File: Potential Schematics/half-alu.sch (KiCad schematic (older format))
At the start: 4 parts

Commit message: Made Full ALU
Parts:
- gave numbers to parts that had none: 4
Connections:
- net 1:2_Multiplexer/Out: now also U2.5; no longer U2.2
- net 2:4_Multiplexer/D0: now also U2.6; no longer U2.3
- net b: now also U2.4; no longer U2.1
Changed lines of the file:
@@
 $Descr A4 11693 8268
 encoding utf-8
-Sheet 3 6
+Sheet 7 22
 Title "Half-ALU"
 Date ""
@@
 $Comp
 L 74LS08 U?
-U 1 1 5B989249
+U 2 1 5B989249
 P 6250 2300
 AR Path="/5B987476/5B989249" Ref="U?"  Part="1"
-AR Path="/5B990C59/5B990C5E/5B989249" Ref="U?"  Part="1"
-F 0 "U?" H 6250 2350 50  0000 C CNN
+AR Path="/5B990C59/5B990C5E/5B989249" Ref="U2"  Part="1"
+AR Path="/5B990C59/5B99C8B8/5B989249" Ref="U21"  Part="4"
+AR Path="/5B990C59/5B99BC00/5B989249" Ref="U5"  Part="2"
+AR Path="/5B990C59/5B99C896/5B989249" Ref="U13"  Part="3"
+F 0 "U5" H 6250 2350 50  0000 C CNN
 F 1 "74LS08" H 6250 2250 50  0000 C CNN
 F 2 "" H 6250 2300 50  0001 C CNN
 F 3 "" H 6250 2300 50  0001 C CNN
-	1    6250 2300
+	2    6250 2300
 	1    0    0    -1
 $EndComp
@@
 P 6250 2800
 AR Path="/5B987476/5B98940C" Ref="U?"  Part="1"
-AR Path="/5B990C59/5B990C5E/5B98940C" Ref="U?"  Part="1"
-F 0 "U?" H 6250 2850 50  0000 C CNN
+AR Path="/5B990C59/5B990C5E/5B98940C" Ref="U3"  Part="1"
+AR Path="/5B990C59/5B99C8B8/5B98940C" Ref="U26"  Part="1"
+AR Path="/5B990C59/5B99BC00/5B98940C" Ref="U11"  Part="1"
+AR Path="/5B990C59/5B99C896/5B98940C" Ref="U19"  Part="1"
+F 0 "U11" H 6250 2850 50  0000 C CNN
 F 1 "74LS32" H 6250 2750 50  0000 C CNN
 F 2 "" H 6250 2800 50  0001 C CNN
@@
 P 6250 3350
 AR Path="/5B987476/5B98B405" Ref="U?"  Part="1"
-AR Path="/5B990C59/5B990C5E/5B98B405" Ref="U?"  Part="1"
-F 0 "U?" H 6300 3400 50  0000 C CNN
+AR Path="/5B990C59/5B990C5E/5B98B405" Ref="U4"  Part="1"
+AR Path="/5B990C59/5B99C8B8/5B98B405" Ref="U27"  Part="1"
+AR Path="/5B990C59/5B99BC00/5B98B405" Ref="U12"  Part="1"
+AR Path="/5B990C59/5B99C896/5B98B405" Ref="U20"  Part="1"
+F 0 "U12" H 6300 3400 50  0000 C CNN
 F 1 "74LS86" H 6300 3300 50  0000 C CNN
 F 2 "" H 6250 3350 50  0001 C CNN
@@
 P 2350 4000
 AR Path="/5B987476/5B98D385" Ref="U?"  Part="1"
-AR Path="/5B990C59/5B990C5E/5B98D385" Ref="U?"  Part="1"
-F 0 "U?" H 2545 4115 50  0000 C CNN
+AR Path="/5B990C59/5B990C5E/5B98D385" Ref="U1"  Part="1"
+AR Path="/5B990C59/5B99C8B8/5B98D385" Ref="U25"  Part="1"
+AR Path="/5B990C59/5B99BC00/5B98D385" Ref="U10"  Part="1"
+AR Path="/5B990C59/5B99C896/5B98D385" Ref="U18"  Part="1"
+F 0 "U10" H 2545 4115 50  0000 C CNN
 F 1 "74LS04" H 2540 3875 50  0000 C CNN
 F 2 "" H 2350 4000 50  0001 C CNN
@@
 $EndSheet
 $Sheet
-S 8100 3300 550  850
+S 8100 3450 550  700
 U 5B98E051
 F0 "2:4_Multiplexer" 60
@@
 Connection ~ 4600 2900
 Wire Wire Line
-	1650 2700 2050 2700
+	1650 2700 5650 2700
 Wire Wire Line
 	2050 2200 2050 3250
 Wire Wire Line
 	2050 2200 5650 2200
-Wire Wire Line
-	2050 2700 5650 2700
 Connection ~ 2050 2700
 Wire Wire Line
@@
 Wire Wire Line
 	5150 4000 5650 4000
+Connection ~ 1900 4000
 $EndSCHEMATC

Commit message: Adding Multiply Devide
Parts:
- U1: symbol 74LS04 -> 4-bit_processor-rescue:74LS04
- U2: symbol 74LS08 -> 4-bit_processor-rescue:74LS08
- U3: symbol 74LS32 -> 4-bit_processor-rescue:74LS32
- U4: symbol 74LS86 -> 4-bit_processor-rescue:74LS86
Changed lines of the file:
@@
-EESchema Schematic File Version 2
-LIBS:power
-LIBS:device
-LIBS:switches
-LIBS:relays
-LIBS:motors
-LIBS:transistors
-LIBS:conn
-LIBS:linear
-LIBS:regul
-LIBS:74xx
-LIBS:cmos4000
-LIBS:adc-dac
-LIBS:memory
-LIBS:xilinx
-LIBS:microcontrollers
-LIBS:dsp
-LIBS:microchip
-LIBS:analog_switches
-LIBS:motorola
-LIBS:texas
-LIBS:intel
-LIBS:audio
-LIBS:interface
-LIBS:digital-audio
-LIBS:philips
-LIBS:display
-LIBS:cypress
-LIBS:siliconi
-LIBS:opto
-LIBS:atmel
-LIBS:contrib
-LIBS:valves
+EESchema Schematic File Version 4
 LIBS:4-bit_processor-cache
-EELAYER 25 0
+EELAYER 26 0
 EELAYER END
 $Descr A4 11693 8268
 encoding utf-8
-Sheet 7 449
+Sheet 4 451
 Title "Half-ALU"
 Date "2018-09-14"
@@
 $EndSheet
 $Comp
-L 74LS08 U?
+L 4-bit_processor-rescue:74LS08 U?
 U 2 1 5B989249
 P 6250 2300
@@
 $EndComp
 $Comp
-L 74LS32 U?
+L 4-bit_processor-rescue:74LS32 U?
 U 1 1 5B98940C
 P 6250 2800
@@
 $EndComp
 $Comp
-L 74LS86 U?
+L 4-bit_processor-rescue:74LS86 U?
 U 1 1 5B98B405
 P 6250 3350
@@
 a
 $Comp
-L 74LS04 U?
+L 4-bit_processor-rescue:74LS04 U?
 U 1 1 5B98D385
 P 2350 4000
@@
 	4600 4200 3950 4200
 Wire Wire Line
-	4600 2400 4600 4400
+	4600 2400 4600 2900
 Wire Wire Line
 	4600 3450 5650 3450
@@
 Connection ~ 4600 2900
 Wire Wire Line
-	1650 2700 5650 2700
-Wire Wire Line
-	2050 2200 2050 3250
+	1650 2700 2050 2700
+Wire Wire Line
+	2050 2200 2050 2700
 Wire Wire Line
 	2050 2200 5650 2200
 Connection ~ 2050 2700
 Wire Wire Line
-	2050 3250 5650 3250
+	2050 3250 5050 3250
 Text HLabel 6700 5500 3    60   Output ~ 0
 Cout
@@
 	5150 4000 5650 4000
 Connection ~ 1900 4000
+Wire Wire Line
+	4600 3450 4600 4200
+Wire Wire Line
+	4600 2900 4600 3450
+Wire Wire Line
+	2050 2700 5650 2700
+Wire Wire Line
+	2050 2700 2050 3250
+Wire Wire Line
+	5050 3250 5650 3250
+Wire Wire Line
+	4600 4200 4600 4400
 $EndSCHEMATC

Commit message: Finished PCB
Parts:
- U1: renamed from U2; footprint (none) -> Daniel_Kopp:DIP-14_300_ELL
- U2: renamed from U1; footprint (none) -> Daniel_Kopp:DIP-14_300_ELL
- U3, U4: footprint (none) -> Daniel_Kopp:DIP-14_300_ELL
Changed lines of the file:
@@
 $Descr A4 11693 8268
 encoding utf-8
-Sheet 4 451
+Sheet 4 456
 Title "Half-ALU"
 Date "2018-09-14"
@@
 P 6250 2300
 AR Path="/5B987476/5B989249" Ref="U?"  Part="1"
-AR Path="/5B990C59/5B990C5E/5B989249" Ref="U2"  Part="1"
-AR Path="/5B990C59/5B99C8B8/5B989249" Ref="U21"  Part="4"
-AR Path="/5B990C59/5B99BC00/5B989249" Ref="U5"  Part="2"
-AR Path="/5B990C59/5B99C896/5B989249" Ref="U13"  Part="3"
-AR Path="/5B9D167A/5B9D1E00/5B990C5E/5B989249" Ref="U5"  Part="2"
-AR Path="/5B9D167A/5B9D1E00/5B99BC00/5B989249" Ref="U5"  Part="2"
-AR Path="/5B9D167A/5B9D1E00/5B99C896/5B989249" Ref="U5"  Part="2"
-AR Path="/5B9D167A/5B9D1E00/5B99C8B8/5B989249" Ref="U5"  Part="2"
-F 0 "U5" H 6250 2350 50  0000 C CNN
+AR Path="/5B990C59/5B990C5E/5B989249" Ref="U?"  Part="1"
+AR Path="/5B990C59/5B99C8B8/5B989249" Ref="U?"  Part="4"
+AR Path="/5B990C59/5B99BC00/5B989249" Ref="U?"  Part="2"
+AR Path="/5B990C59/5B99C896/5B989249" Ref="U?"  Part="3"
+AR Path="/5B9D167A/5B9D1E00/5B990C5E/5B989249" Ref="U1"  Part="2"
+AR Path="/5B9D167A/5B9D1E00/5B99BC00/5B989249" Ref="U5"  Part="3"
+AR Path="/5B9D167A/5B9D1E00/5B99C896/5B989249" Ref="U10"  Part="4"
+AR Path="/5B9D167A/5B9D1E00/5B99C8B8/5B989249" Ref="U19"  Part="1"
+F 0 "U1" H 6250 2350 50  0000 C CNN
 F 1 "74LS08" H 6250 2250 50  0000 C CNN
-F 2 "" H 6250 2300 50  0001 C CNN
+F 2 "Daniel_Kopp:DIP-14_300_ELL" H 6250 2300 50  0001 C CNN
 F 3 "" H 6250 2300 50  0001 C CNN
 	2    6250 2300
@@
 P 6250 2800
 AR Path="/5B987476/5B98940C" Ref="U?"  Part="1"
-AR Path="/5B990C59/5B990C5E/5B98940C" Ref="U3"  Part="1"
-AR Path="/5B990C59/5B99C8B8/5B98940C" Ref="U26"  Part="1"
-AR Path="/5B990C59/5B99BC00/5B98940C" Ref="U11"  Part="1"
-AR Path="/5B990C59/5B99C896/5B98940C" Ref="U19"  Part="1"
-AR Path="/5B9D167A/5B9D1E00/5B990C5E/5B98940C" Ref="U11"  Part="1"
-AR Path="/5B9D167A/5B9D1E00/5B99BC00/5B98940C" Ref="U11"  Part="1"
-AR Path="/5B9D167A/5B9D1E00/5B99C896/5B98940C" Ref="U11"  Part="1"
-AR Path="/5B9D167A/5B9D1E00/5B99C8B8/5B98940C" Ref="U11"  Part="1"
-F 0 "U11" H 6250 2850 50  0000 C CNN
+AR Path="/5B990C59/5B990C5E/5B98940C" Ref="U?"  Part="1"
+AR Path="/5B990C59/5B99C8B8/5B98940C" Ref="U?"  Part="1"
+AR Path="/5B990C59/5B99BC00/5B98940C" Ref="U?"  Part="1"
+AR Path="/5B990C59/5B99C896/5B98940C" Ref="U?"  Part="1"
+AR Path="/5B9D167A/5B9D1E00/5B990C5E/5B98940C" Ref="U3"  Part="1"
+AR Path="/5B9D167A/5B9D1E00/5B99BC00/5B98940C" Ref="U8"  Part="2"
+AR Path="/5B9D167A/5B9D1E00/5B99C896/5B98940C" Ref="U13"  Part="3"
+AR Path="/5B9D167A/5B9D1E00/5B99C8B8/5B98940C" Ref="U17"  Part="4"
+F 0 "U3" H 6250 2850 50  0000 C CNN
 F 1 "74LS32" H 6250 2750 50  0000 C CNN
-F 2 "" H 6250 2800 50  0001 C CNN
+F 2 "Daniel_Kopp:DIP-14_300_ELL" H 6250 2800 50  0001 C CNN
 F 3 "" H 6250 2800 50  0001 C CNN
 	1    6250 2800
@@
 P 6250 3350
 AR Path="/5B987476/5B98B405" Ref="U?"  Part="1"
-AR Path="/5B990C59/5B990C5E/5B98B405" Ref="U4"  Part="1"
-AR Path="/5B990C59/5B99C8B8/5B98B405" Ref="U27"  Part="1"
-AR Path="/5B990C59/5B99BC00/5B98B405" Ref="U12"  Part="1"
-AR Path="/5B990C59/5B99C896/5B98B405" Ref="U20"  Part="1"
-AR Path="/5B9D167A/5B9D1E00/5B990C5E/5B98B405" Ref="U12"  Part="1"
-AR Path="/5B9D167A/5B9D1E00/5B99BC00/5B98B405" Ref="U12"  Part="1"
-AR Path="/5B9D167A/5B9D1E00/5B99C896/5B98B405" Ref="U12"  Part="1"
-AR Path="/5B9D167A/5B9D1E00/5B99C8B8/5B98B405" Ref="U12"  Part="1"
-F 0 "U12" H 6300 3400 50  0000 C CNN
+AR Path="/5B990C59/5B990C5E/5B98B405" Ref="U?"  Part="1"
+AR Path="/5B990C59/5B99C8B8/5B98B405" Ref="U?"  Part="1"
+AR Path="/5B990C59/5B99BC00/5B98B405" Ref="U?"  Part="1"
+AR Path="/5B990C59/5B99C896/5B98B405" Ref="U?"  Part="1"
+AR Path="/5B9D167A/5B9D1E00/5B990C5E/5B98B405" Ref="U4"  Part="1"
+AR Path="/5B9D167A/5B9D1E00/5B99BC00/5B98B405" Ref="U9"  Part="1"
+AR Path="/5B9D167A/5B9D1E00/5B99C896/5B98B405" Ref="U14"  Part="1"
+AR Path="/5B9D167A/5B9D1E00/5B99C8B8/5B98B405" Ref="U20"  Part="1"
+F 0 "U4" H 6300 3400 50  0000 C CNN
 F 1 "74LS86" H 6300 3300 50  0000 C CNN
-F 2 "" H 6250 3350 50  0001 C CNN
+F 2 "Daniel_Kopp:DIP-14_300_ELL" H 6250 3350 50  0001 C CNN
 F 3 "" H 6250 3350 50  0001 C CNN
 	1    6250 3350
@@
 P 2350 4000
 AR Path="/5B987476/5B98D385" Ref="U?"  Part="1"
-AR Path="/5B990C59/5B990C5E/5B98D385" Ref="U1"  Part="1"
-AR Path="/5B990C59/5B99C8B8/5B98D385" Ref="U25"  Part="1"
-AR Path="/5B990C59/5B99BC00/5B98D385" Ref="U10"  Part="1"
-AR Path="/5B990C59/5B99C896/5B98D385" Ref="U18"  Part="1"
-AR Path="/5B9D167A/5B9D1E00/5B990C5E/5B98D385" Ref="U10"  Part="1"
-AR Path="/5B9D167A/5B9D1E00/5B99BC00/5B98D385" Ref="U10"  Part="1"
-AR Path="/5B9D167A/5B9D1E00/5B99C896/5B98D385" Ref="U10"  Part="1"
-AR Path="/5B9D167A/5B9D1E00/5B99C8B8/5B98D385" Ref="U10"  Part="1"
-F 0 "U10" H 2545 4115 50  0000 C CNN
+AR Path="/5B990C59/5B990C5E/5B98D385" Ref="U?"  Part="1"
+AR Path="/5B990C59/5B99C8B8/5B98D385" Ref="U?"  Part="1"
+AR Path="/5B990C59/5B99BC00/5B98D385" Ref="U?"  Part="1"
+AR Path="/5B990C59/5B99C896/5B98D385" Ref="U?"  Part="1"
+AR Path="/5B9D167A/5B9D1E00/5B990C5E/5B98D385" Ref="U2"  Part="1"
+AR Path="/5B9D167A/5B9D1E00/5B99BC00/5B98D385" Ref="U2"  Part="5"
+AR Path="/5B9D167A/5B9D1E00/5B99C896/5B98D385" Ref="U11"  Part="3"
+AR Path="/5B9D167A/5B9D1E00/5B99C8B8/5B98D385" Ref="U18"  Part="1"
+F 0 "U2" H 2545 4115 50  0000 C CNN
 F 1 "74LS04" H 2540 3875 50  0000 C CNN
-F 2 "" H 2350 4000 50  0001 C CNN
+F 2 "Daniel_Kopp:DIP-14_300_ELL" H 2350 4000 50  0001 C CNN
 F 3 "" H 2350 4000 50  0001 C CNN
 	1    2350 4000

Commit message: Working on Multiplier
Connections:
- net 1:2_Multiplexer/Out: now also U1.2, U3.13; no longer U1.5, U3.2
- net 2:4_Multiplexer/D0: now also U1.3; no longer U1.6
- net 2:4_Multiplexer/D1: now also U3.11; no longer U3.3
- net b: now also U1.1, U3.12; no longer U1.4, U3.1
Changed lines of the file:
@@
 $Descr A4 11693 8268
 encoding utf-8
-Sheet 4 456
+Sheet 16 458
 Title "Half-ALU"
 Date "2018-09-14"
@@
 $Comp
 L 4-bit_processor-rescue:74LS08 U?
-U 2 1 5B989249
+U 1 1 5B989249
 P 6250 2300
 AR Path="/5B987476/5B989249" Ref="U?"  Part="1"
@@
 AR Path="/5B9D167A/5B9D1E00/5B99C896/5B989249" Ref="U10"  Part="4"
 AR Path="/5B9D167A/5B9D1E00/5B99C8B8/5B989249" Ref="U19"  Part="1"
-F 0 "U1" H 6250 2350 50  0000 C CNN
+F 0 "U19" H 6250 2350 50  0000 C CNN
 F 1 "74LS08" H 6250 2250 50  0000 C CNN
 F 2 "Daniel_Kopp:DIP-14_300_ELL" H 6250 2300 50  0001 C CNN
 F 3 "" H 6250 2300 50  0001 C CNN
-	2    6250 2300
+	1    6250 2300
 	1    0    0    -1
 $EndComp
 $Comp
 L 4-bit_processor-rescue:74LS32 U?
-U 1 1 5B98940C
+U 4 1 5B98940C
 P 6250 2800
 AR Path="/5B987476/5B98940C" Ref="U?"  Part="1"
@@
 AR Path="/5B9D167A/5B9D1E00/5B99C896/5B98940C" Ref="U13"  Part="3"
 AR Path="/5B9D167A/5B9D1E00/5B99C8B8/5B98940C" Ref="U17"  Part="4"
-F 0 "U3" H 6250 2850 50  0000 C CNN
+F 0 "U17" H 6250 2850 50  0000 C CNN
 F 1 "74LS32" H 6250 2750 50  0000 C CNN
 F 2 "Daniel_Kopp:DIP-14_300_ELL" H 6250 2800 50  0001 C CNN
 F 3 "" H 6250 2800 50  0001 C CNN
-	1    6250 2800
+	4    6250 2800
 	1    0    0    -1
 $EndComp
@@
 AR Path="/5B9D167A/5B9D1E00/5B99C896/5B98B405" Ref="U14"  Part="1"
 AR Path="/5B9D167A/5B9D1E00/5B99C8B8/5B98B405" Ref="U20"  Part="1"
-F 0 "U4" H 6300 3400 50  0000 C CNN
+F 0 "U20" H 6300 3400 50  0000 C CNN
 F 1 "74LS86" H 6300 3300 50  0000 C CNN
 F 2 "Daniel_Kopp:DIP-14_300_ELL" H 6250 3350 50  0001 C CNN
@@
 AR Path="/5B9D167A/5B9D1E00/5B99C896/5B98D385" Ref="U11"  Part="3"
 AR Path="/5B9D167A/5B9D1E00/5B99C8B8/5B98D385" Ref="U18"  Part="1"
-F 0 "U2" H 2545 4115 50  0000 C CNN
+F 0 "U18" H 2545 4115 50  0000 C CNN
 F 1 "74LS04" H 2540 3875 50  0000 C CNN
 F 2 "Daniel_Kopp:DIP-14_300_ELL" H 2350 4000 50  0001 C CNN

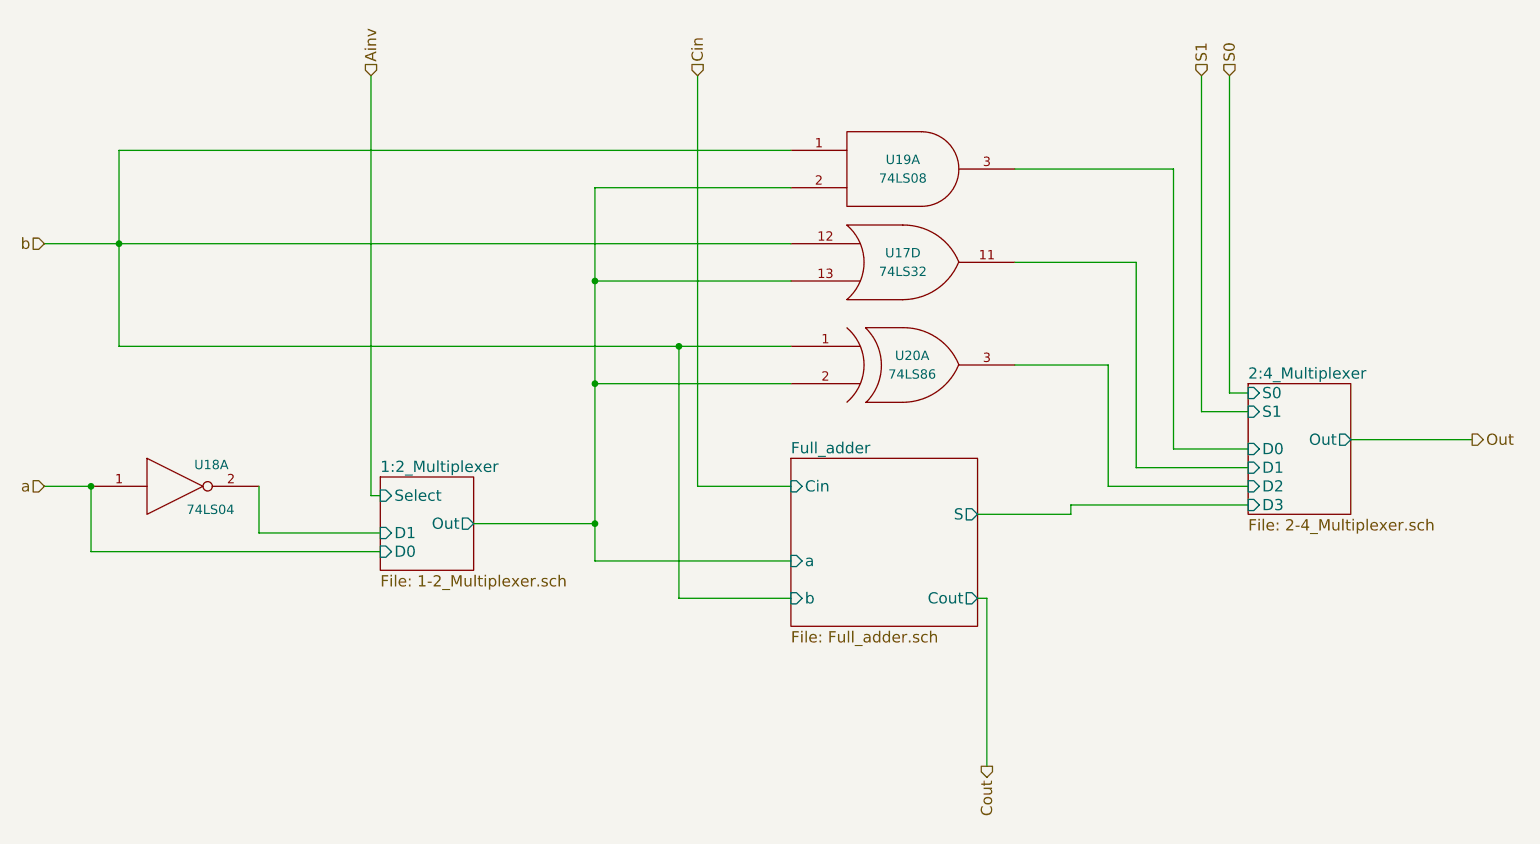
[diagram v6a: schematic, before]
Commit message: Updated overview of Schematic
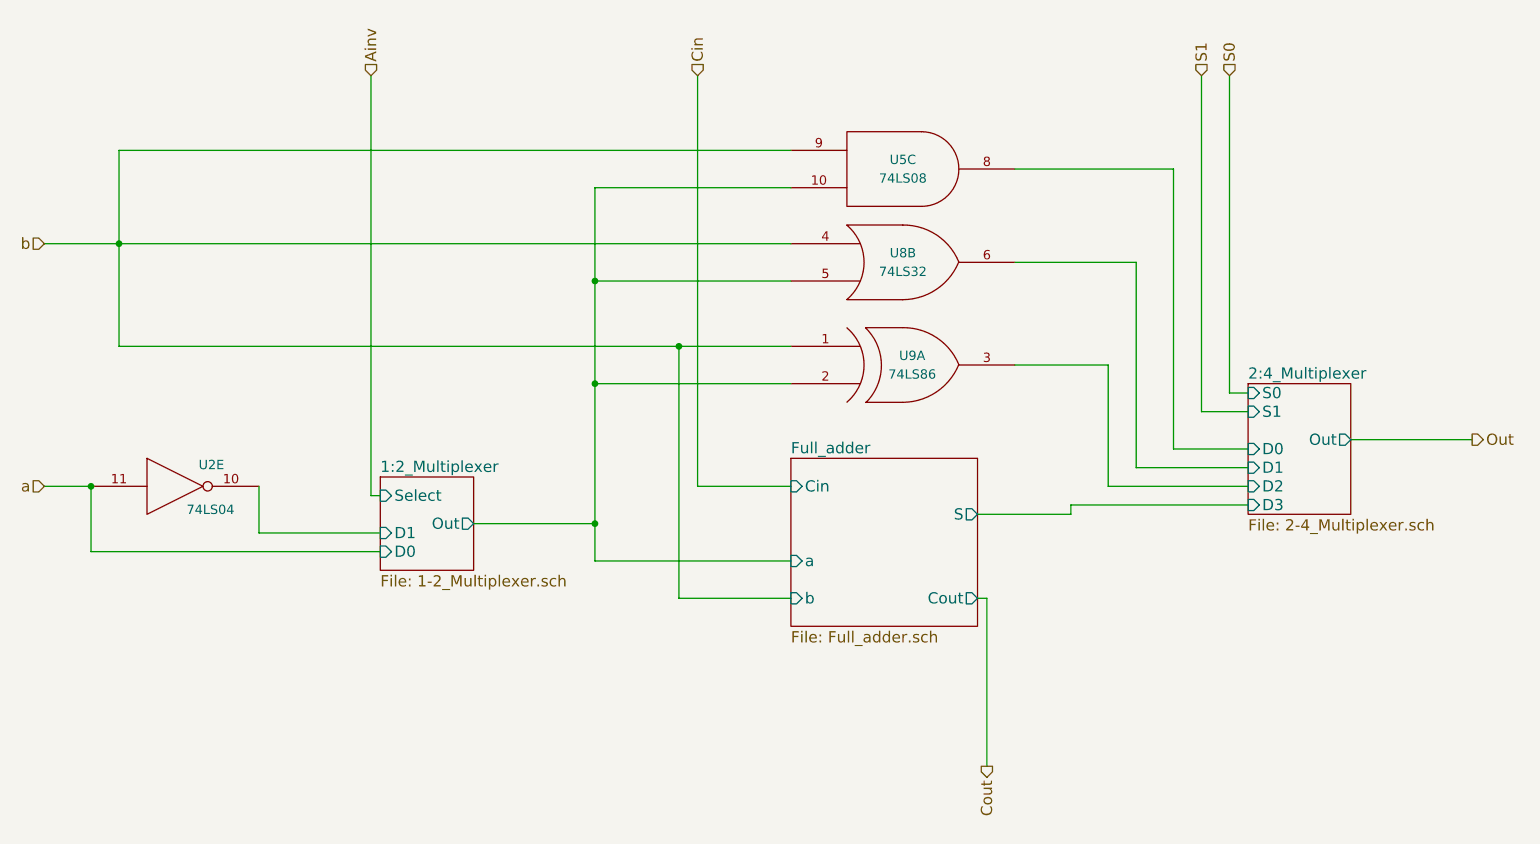
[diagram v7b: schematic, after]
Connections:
- net 1:2_Multiplexer/D1: now also U2.10; no longer U2.2
- net 1:2_Multiplexer/Out: now also U1.10, U3.5; no longer U1.2, U3.13
- net 2:4_Multiplexer/D0: now also U1.8; no longer U1.3
- net 2:4_Multiplexer/D1: now also U3.6; no longer U3.11
- net a: now also U2.11; no longer U2.1
- net b: now also U1.9, U3.4; no longer U1.1, U3.12
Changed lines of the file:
@@
 $Descr A4 11693 8268
 encoding utf-8
-Sheet 16 467
+Sheet 8 902
 Title "Half-ALU"
 Date "2018-09-14"
@@
 $Comp
 L 4-bit_processor-rescue:74LS08 U?
-U 1 1 5B989249
+U 3 1 5B989249
 P 6250 2300
 AR Path="/5B987476/5B989249" Ref="U?"  Part="1"
@@
 AR Path="/5B9D167A/5B9D1E00/5B99C896/5B989249" Ref="U10"  Part="4"
 AR Path="/5B9D167A/5B9D1E00/5B99C8B8/5B989249" Ref="U19"  Part="1"
-F 0 "U19" H 6250 2350 50  0000 C CNN
+F 0 "U5" H 6250 2350 50  0000 C CNN
 F 1 "74LS08" H 6250 2250 50  0000 C CNN
 F 2 "Daniel_Kopp:DIP-14_300_ELL" H 6250 2300 50  0001 C CNN
 F 3 "" H 6250 2300 50  0001 C CNN
-	1    6250 2300
+	3    6250 2300
 	1    0    0    -1
 $EndComp
 $Comp
 L 4-bit_processor-rescue:74LS32 U?
-U 4 1 5B98940C
+U 2 1 5B98940C
 P 6250 2800
 AR Path="/5B987476/5B98940C" Ref="U?"  Part="1"
@@
 AR Path="/5B9D167A/5B9D1E00/5B99C896/5B98940C" Ref="U13"  Part="3"
 AR Path="/5B9D167A/5B9D1E00/5B99C8B8/5B98940C" Ref="U17"  Part="4"
-F 0 "U17" H 6250 2850 50  0000 C CNN
+F 0 "U8" H 6250 2850 50  0000 C CNN
 F 1 "74LS32" H 6250 2750 50  0000 C CNN
 F 2 "Daniel_Kopp:DIP-14_300_ELL" H 6250 2800 50  0001 C CNN
 F 3 "" H 6250 2800 50  0001 C CNN
-	4    6250 2800
+	2    6250 2800
 	1    0    0    -1
 $EndComp
@@
 AR Path="/5B9D167A/5B9D1E00/5B99C896/5B98B405" Ref="U14"  Part="1"
 AR Path="/5B9D167A/5B9D1E00/5B99C8B8/5B98B405" Ref="U20"  Part="1"
-F 0 "U20" H 6300 3400 50  0000 C CNN
+F 0 "U9" H 6300 3400 50  0000 C CNN
 F 1 "74LS86" H 6300 3300 50  0000 C CNN
 F 2 "Daniel_Kopp:DIP-14_300_ELL" H 6250 3350 50  0001 C CNN
@@
 $Comp
 L 4-bit_processor-rescue:74LS04 U?
-U 1 1 5B98D385
+U 5 1 5B98D385
 P 2350 4000
 AR Path="/5B987476/5B98D385" Ref="U?"  Part="1"
@@
 AR Path="/5B9D167A/5B9D1E00/5B99C896/5B98D385" Ref="U11"  Part="3"
 AR Path="/5B9D167A/5B9D1E00/5B99C8B8/5B98D385" Ref="U18"  Part="1"
-F 0 "U18" H 2545 4115 50  0000 C CNN
+F 0 "U2" H 2545 4115 50  0000 C CNN
 F 1 "74LS04" H 2540 3875 50  0000 C CNN
 F 2 "Daniel_Kopp:DIP-14_300_ELL" H 2350 4000 50  0001 C CNN
 F 3 "" H 2350 4000 50  0001 C CNN
-	1    2350 4000
+	5    2350 4000
 	1    0    0    -1
 $EndComp
